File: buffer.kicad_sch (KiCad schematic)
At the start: 8 parts, among them J13 V_SIG, J14 Conn_01x02_Pin, J15 VSIG_BUF, U5 BUF634AIDR

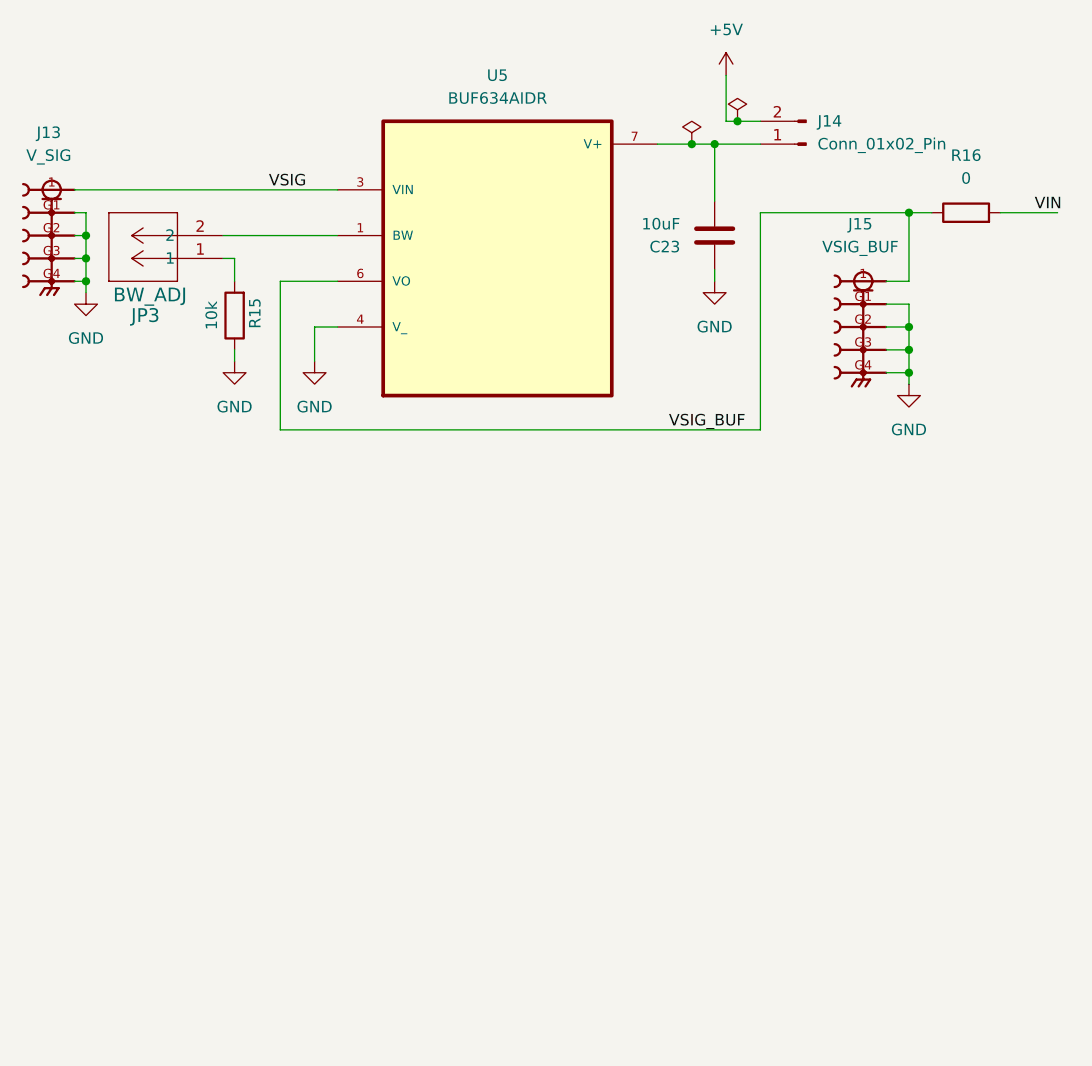
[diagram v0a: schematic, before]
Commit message: changed buffer for better headroom
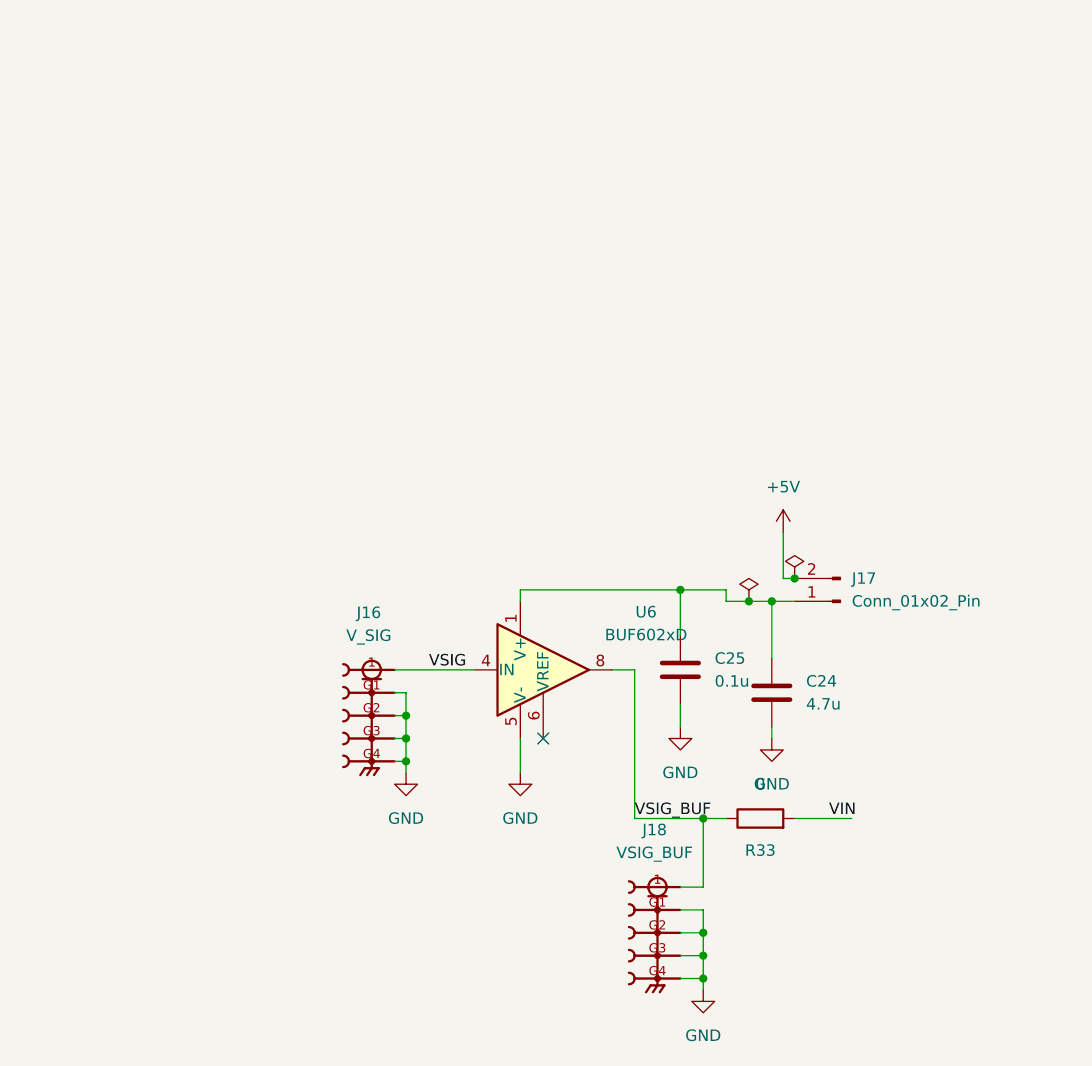
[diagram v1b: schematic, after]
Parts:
- removed C23: 10uF, Capacitor_SMD:C_0805_2012Metric_Pad1.18x1.45mm_HandSolder, symbol Device:C
- removed J13: V_SIG, TPS7A7001_Evaluation_Board_footprint_lib:SAMTEC_SMA-J-P-H-ST-TH1, symbol SMA-J-P-H-ST-TH1:SMA-J-P-H-ST-TH1
- removed J14: Conn_01x02_Pin, Package_DIP:DIP-20_W7.62mm, symbol Connector:Conn_01x02_Pin
- removed J15: VSIG_BUF, SMA_J_P_H_ST_TH1:SAMTEC_SMA-J-P-H-ST-TH1, symbol SMA-J-P-H-ST-TH1:SMA-J-P-H-ST-TH1
- removed JP3: BW_ADJ, TPS7A7001_Evaluation_Board_footprint_lib:CONN_PxC02S_SUL, symbol PEC02SAAN:PEC02SAAN
- removed R15: 10k, Resistor_SMD:R_0805_2012Metric_Pad1.20x1.40mm_HandSolder, symbol Device:R
- removed R16: 0, Resistor_SMD:R_0805_2012Metric_Pad1.20x1.40mm_HandSolder, symbol Device:R
- removed U5: BUF634AIDR, TPS7A7001_Evaluation_Board_footprint_lib:SOIC127P599X175-8N, symbol TPS7A7001_Evaluation_Board_symbol_lib:BUF634AIDR
- added C24: 4.7u, Capacitor_SMD:C_0805_2012Metric_Pad1.18x1.45mm_HandSolder, symbol Device:C
- added C25: 0.1u, Capacitor_SMD:C_0805_2012Metric_Pad1.18x1.45mm_HandSolder, symbol Device:C
- added J16: V_SIG, TPS7A7001_Evaluation_Board_footprint_lib:SAMTEC_SMA-J-P-H-ST-TH1, symbol SMA-J-P-H-ST-TH1:SMA-J-P-H-ST-TH1
- added J17: Conn_01x02_Pin, Package_DIP:DIP-20_W7.62mm, symbol Connector:Conn_01x02_Pin
- added J18: VSIG_BUF, SMA_J_P_H_ST_TH1:SAMTEC_SMA-J-P-H-ST-TH1, symbol SMA-J-P-H-ST-TH1:SMA-J-P-H-ST-TH1
- added R33: 0, Resistor_SMD:R_0805_2012Metric_Pad1.20x1.40mm_HandSolder, symbol Device:R
- added U6: BUF602xD, Package_SO:SOIC-8_3.9x4.9mm_P1.27mm, symbol Amplifier_Buffer:BUF602xD
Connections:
- net +5V: now also J17.2 (Pin_2)
- net GND: now also C24.1, C25.1, J16.G1, J16.G2, J16.G3, J16.G4, J18.G1, J18.G2, J18.G3, J18.G4, U6.5 (V-)
- net VIN: now also R33.2
- net VSIG: now also J16.1, U6.4 (IN)
- net VSIG_BUF: now also J18.1, R33.1, U6.8
- new net: C24.2, C25.2, J17.1 (Pin_1), U6.1 (V+)
- no-connect marks 0 -> 1
